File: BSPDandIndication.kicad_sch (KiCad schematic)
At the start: 50 parts, among them J5 12VTelem, K1 FINDER-36.11, U1 LM1117-5.0, U2 LM1117-5.0, U5 NE555D

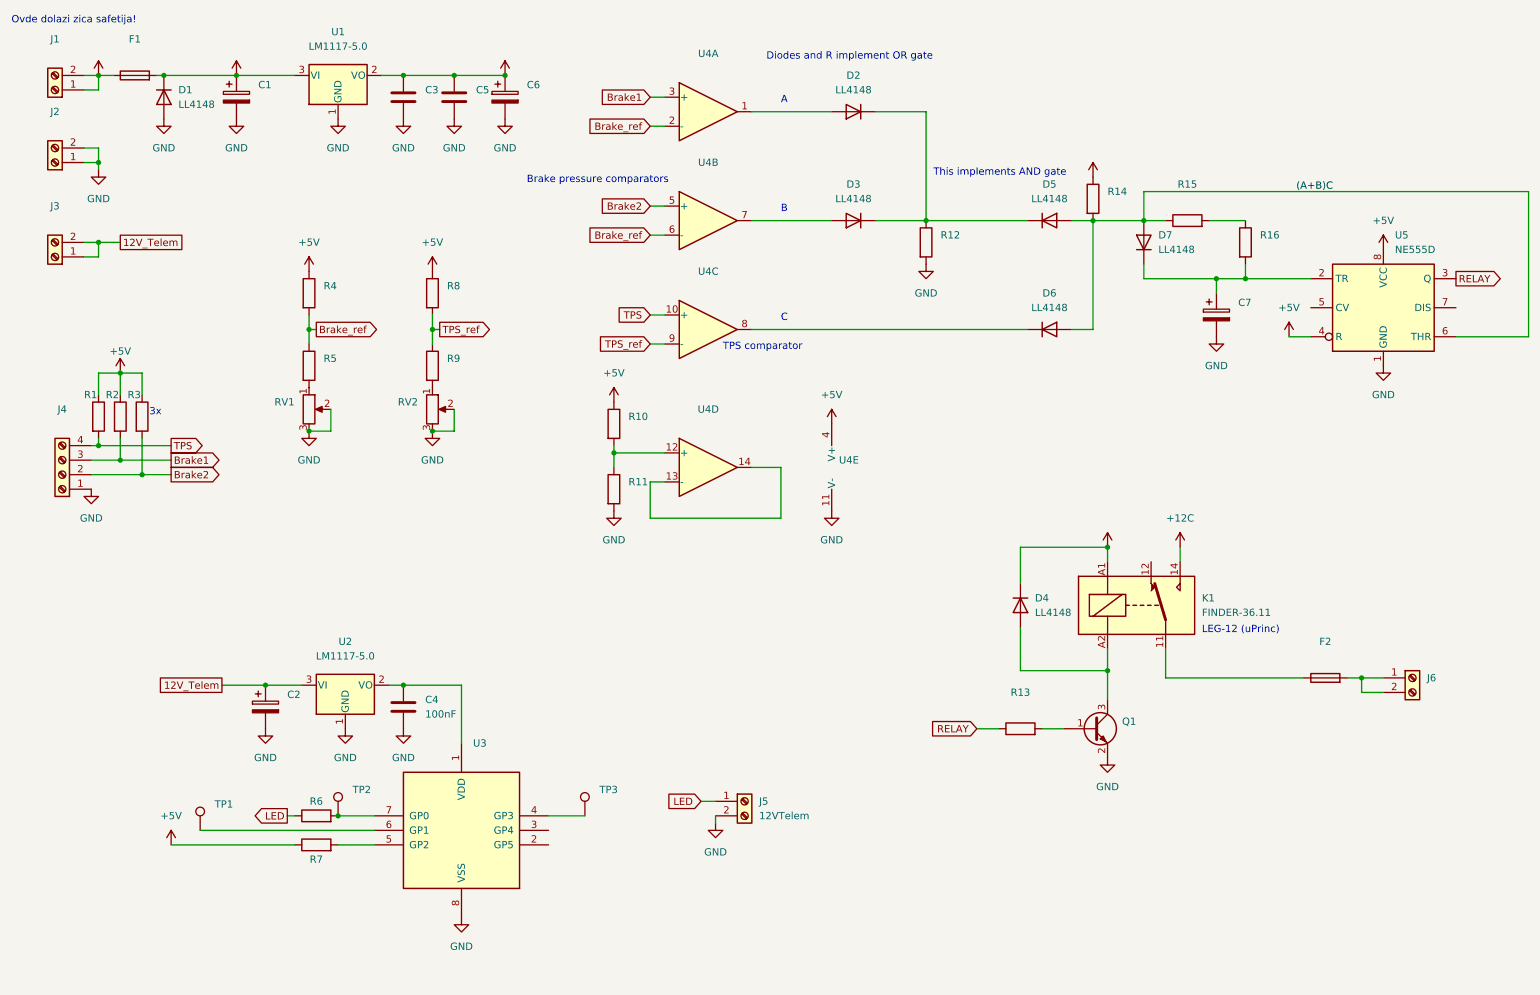
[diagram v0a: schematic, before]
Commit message: Update J5 value
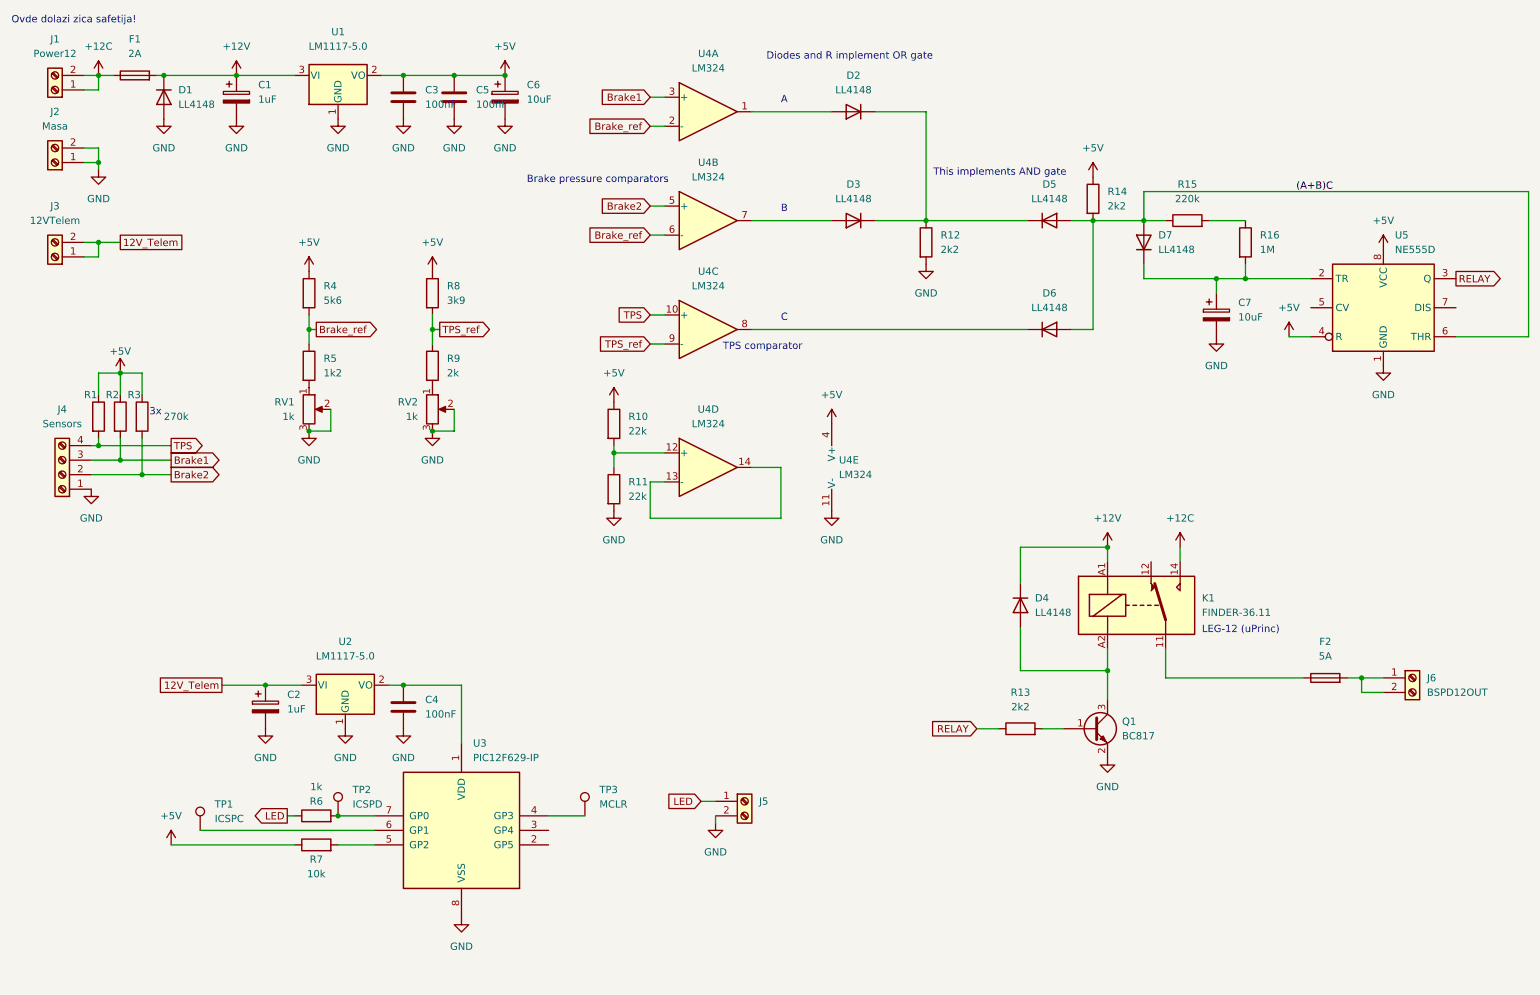
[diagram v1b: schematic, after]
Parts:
- C1, C2: value (none) -> 1uF; footprint (none) -> Capacitor_Tantalum_SMD:CP_EIA-3216-18_Kemet-A_Pad1.58x1.35mm_HandSolder
- C3, C5: value (none) -> 100nF; footprint (none) -> Capacitor_SMD:C_1206_3216Metric_Pad1.33x1.80mm_HandSolder
- C4: footprint (none) -> Capacitor_SMD:C_1206_3216Metric_Pad1.33x1.80mm_HandSolder
- C6, C7: value (none) -> 10uF; footprint (none) -> Capacitor_Tantalum_SMD:CP_EIA-3216-18_Kemet-A_Pad1.58x1.35mm_HandSolder
- F1: value (none) -> 2A; footprint (none) -> Fuse:Fuse_2512_6332Metric_Pad1.52x3.35mm_HandSolder
- F2: value (none) -> 5A; footprint (none) -> Fuse:Fuseholder_Cylinder-5x20mm_Schurter_0031_8201_Horizontal_Open
- J1: value (none) -> Power12; footprint (none) -> AK3001:AK300_1x02_P5.00mm_45-Degree
- J2: value (none) -> Masa; footprint (none) -> AK3001:AK300_1x02_P5.00mm_45-Degree
- J3: value (none) -> 12VTelem; footprint (none) -> AK3001:AK300_1x02_P5.00mm_45-Degree
- J4: value (none) -> Sensors; footprint (none) -> AK3001:AK3001_1x04_P5.00mm_45-Degree
- J5: value 12VTelem -> (none); footprint (none) -> AK3001:AK300_1x02_P5.00mm_45-Degree
- J6: value (none) -> BSPD12OUT; footprint (none) -> AK3001:AK300_1x02_P5.00mm_45-Degree
- Q1: value (none) -> BC817; footprint (none) -> Package_TO_SOT_SMD:SOT-23
- R1, R2, R3: value (none) -> 270k; footprint (none) -> Resistor_SMD:R_1206_3216Metric_Pad1.30x1.75mm_HandSolder
- R10, R11: value (none) -> 22k; footprint (none) -> Resistor_SMD:R_1206_3216Metric_Pad1.30x1.75mm_HandSolder
- R12, R13, R14: value (none) -> 2k2; footprint (none) -> Resistor_SMD:R_1206_3216Metric_Pad1.30x1.75mm_HandSolder
- R15: value (none) -> 220k; footprint (none) -> Resistor_SMD:R_1206_3216Metric_Pad1.30x1.75mm_HandSolder
- R16: value (none) -> 1M; footprint (none) -> Resistor_SMD:R_1206_3216Metric_Pad1.30x1.75mm_HandSolder
- R4: value (none) -> 5k6; footprint (none) -> Resistor_SMD:R_1206_3216Metric_Pad1.30x1.75mm_HandSolder
- R5: value (none) -> 1k2; footprint (none) -> Resistor_SMD:R_1206_3216Metric_Pad1.30x1.75mm_HandSolder
- R6: value (none) -> 1k; footprint (none) -> Resistor_SMD:R_1206_3216Metric_Pad1.30x1.75mm_HandSolder
- R7: value (none) -> 10k; footprint (none) -> Resistor_SMD:R_1206_3216Metric_Pad1.30x1.75mm_HandSolder
- R8: value (none) -> 3k9; footprint (none) -> Resistor_SMD:R_1206_3216Metric_Pad1.30x1.75mm_HandSolder
- R9: value (none) -> 2k; footprint (none) -> Resistor_SMD:R_1206_3216Metric_Pad1.30x1.75mm_HandSolder
- RV1, RV2: value (none) -> 1k; footprint (none) -> Potentiometer_SMD:Potentiometer_Vishay_TS53YL_Vertical
- TP1: value (none) -> ICSPC; footprint (none) -> TestPoint:TestPoint_Pad_2.5x2.5mm
- TP2: value (none) -> ICSPD; footprint (none) -> TestPoint:TestPoint_Pad_2.5x2.5mm
- TP3: value (none) -> MCLR; footprint (none) -> TestPoint:TestPoint_Pad_2.5x2.5mm
- U1, U2: footprint (none) -> Package_TO_SOT_SMD:SOT-223
- U3: value (none) -> PIC12F629-IP; footprint (none) -> Package_DIP:DIP-8_W7.62mm
- U4: value (none) -> LM324; footprint (none) -> Package_SO:SO-14_3.9x8.65mm_P1.27mm
- U4: value (none) -> LM324
